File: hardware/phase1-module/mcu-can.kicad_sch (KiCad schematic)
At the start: 0 parts

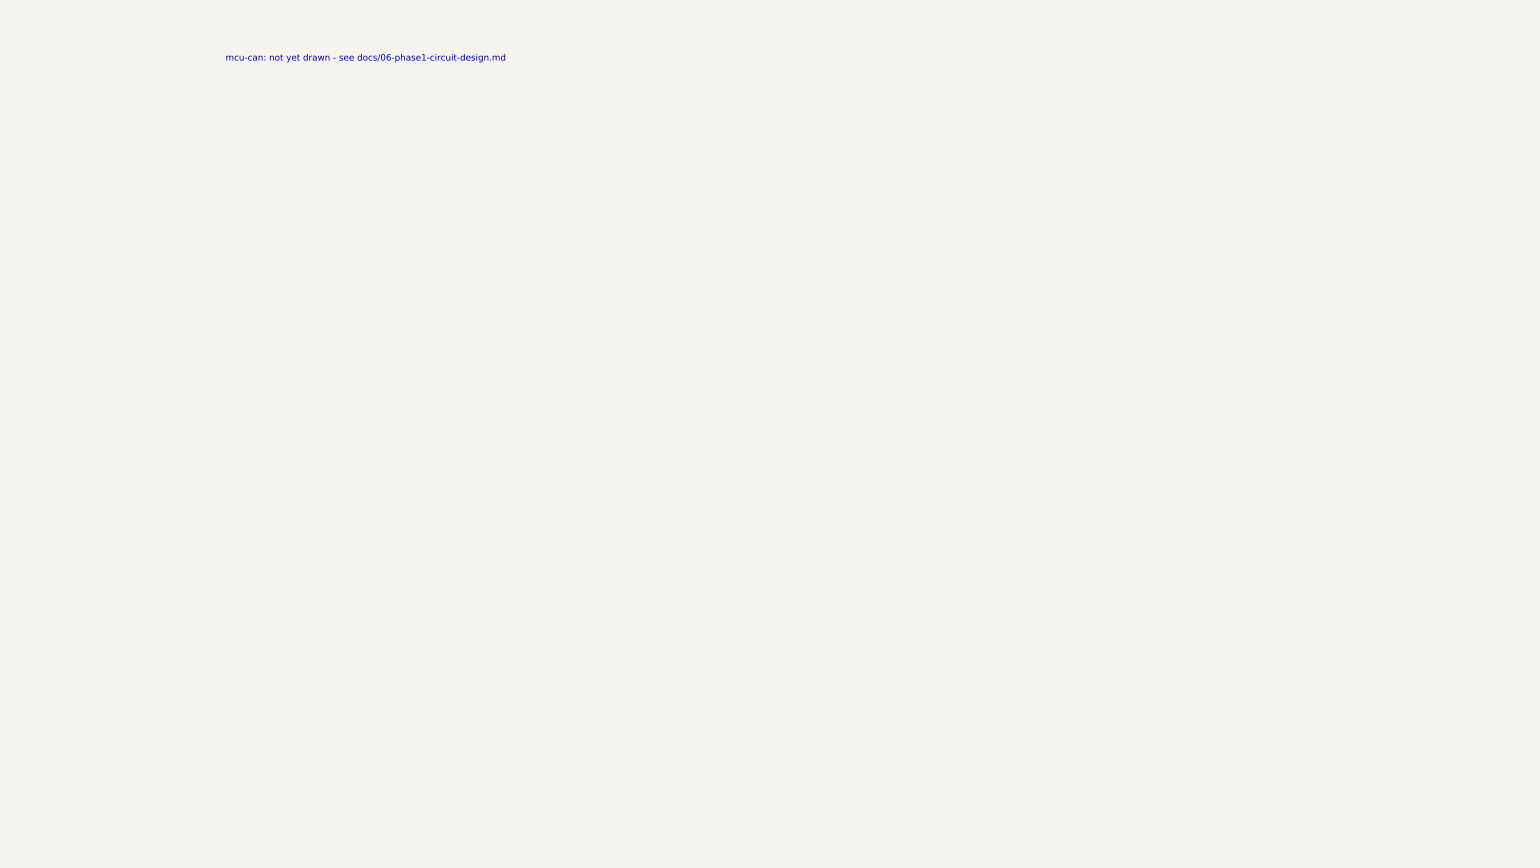
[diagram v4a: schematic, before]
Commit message: Complete Phase-1 schematic: all six remaining sheets, netlist-verified
- power-stage: LM5145 @350kHz (RT 28.7K per ds eq.3), RDS(on) valley
  ILIM 365R->SW, UVLO divider, EN kill chain (NOT(HW_EN) OR PS_OFF via
  Q5/Q6 + diode-OR), Type-III comp starting values, SYNCIN as DEM/FPWM
- sensing: 2m shunt, INA240A3 -> CC loop, INA228 telemetry, /8 divider,
  NT1 single AGND-PGND tie
- disconnect: back-to-back FETs + LTC7004, INP = OUT_REQ AND NOT(kill)
  AND NOT(OVP); TLV7011 + Q9 trips at 22.25V
- aux-rails: LMR36015 (5.016V) -> NCP1117 3V3
- mcu-can: STM32G431CBT6 fully pinned; I2C moved to I2C2/PA8-PA9 (PB8
  is the BOOT0 strap - pullup there would boot the ROM loader), BOOT0
  strapped low, OUT_REQ on PB14 (PB4 NJTRST reset pull-up), 8MHz
  crystal for CAN, TCAN1042 (VCC 5V, VIO 3V3)
- io: fused input + SMBJ33A TVS, output, backplane header, fan switch
  (1N4148W flyback orientation corrected: pin 1 = cathode)
- checker: duplicate-ref detection + global/local split-net detection;
  caught duplicate C62 and the LMR36015 FB-pin placement collision

Co-Authored-By: Claude Fable 5 <noreply@anthropic.com>
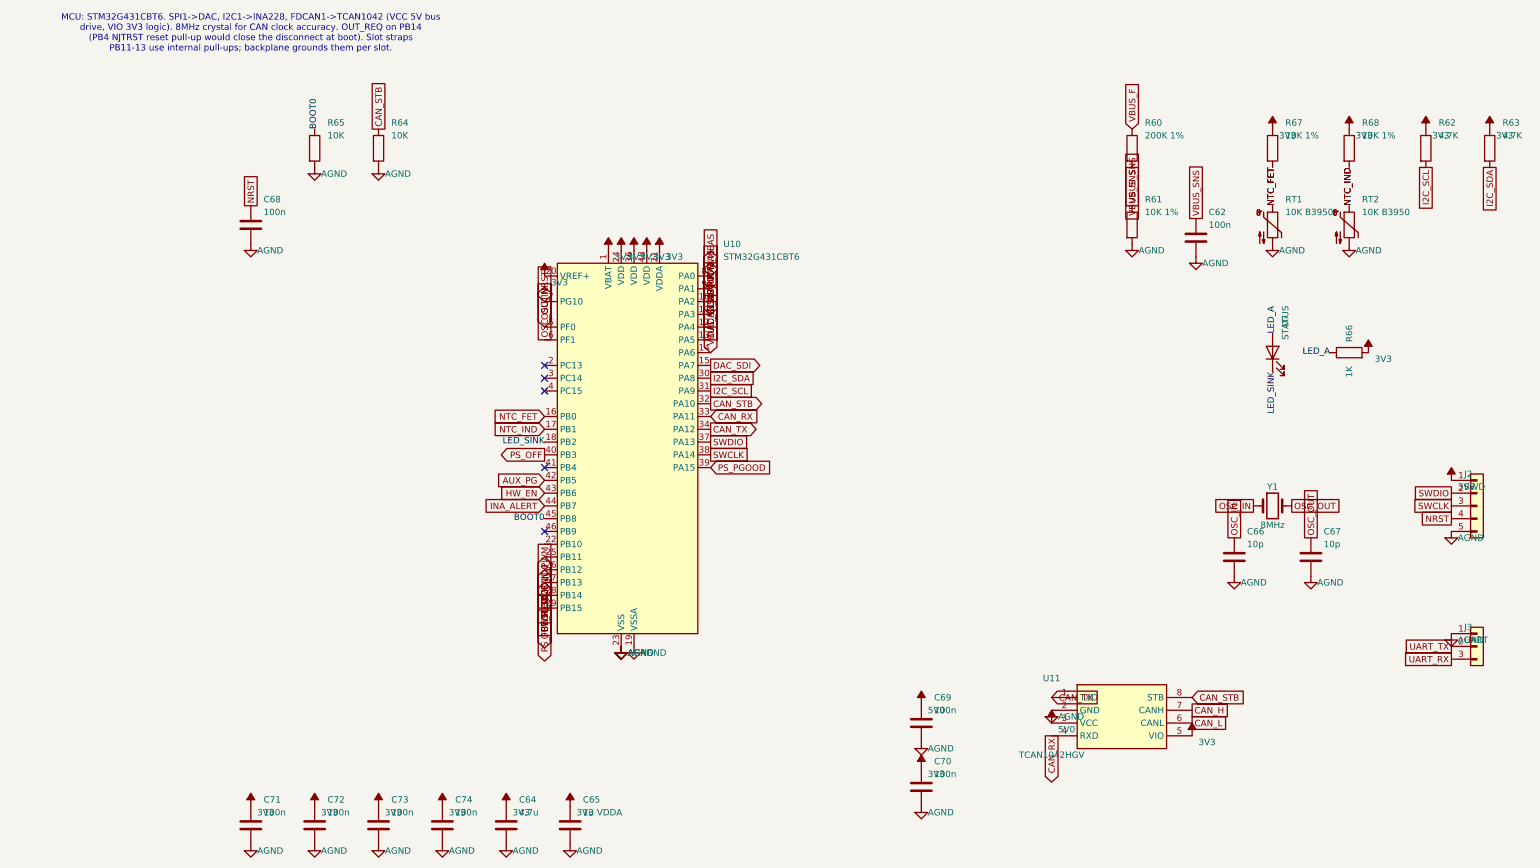
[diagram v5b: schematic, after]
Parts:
- added C62, C68, C69, C70, C71, C72, C73, C74: 100n, Capacitor_SMD:C_0402_1005Metric, symbol Device:C
- added C64: 4.7u, Capacitor_SMD:C_0402_1005Metric, symbol Device:C
- added C65: 1u VDDA, Capacitor_SMD:C_0402_1005Metric, symbol Device:C
- added C66, C67: 10p, Capacitor_SMD:C_0402_1005Metric, symbol Device:C
- added D7: STATUS, LED_SMD:LED_0603_1608Metric, symbol Device:LED
- added J2: SWD, Connector_PinHeader_2.54mm:PinHeader_1x05_P2.54mm_Vertical, symbol Connector_Generic:Conn_01x05
- added J3: UART, Connector_PinHeader_2.54mm:PinHeader_1x03_P2.54mm_Vertical, symbol Connector_Generic:Conn_01x03
- added R60: 200K 1%, Resistor_SMD:R_0402_1005Metric, symbol Device:R
- added R61, R67, R68: 10K 1%, Resistor_SMD:R_0402_1005Metric, symbol Device:R
- added R62, R63: 4.7K, Resistor_SMD:R_0402_1005Metric, symbol Device:R
- added R64, R65: 10K, Resistor_SMD:R_0402_1005Metric, symbol Device:R
- added R66: 1K, Resistor_SMD:R_0402_1005Metric, symbol Device:R
- added RT1, RT2: 10K B3950, Resistor_SMD:R_0603_1608Metric, symbol Device:Thermistor_NTC
- added U10: STM32G431CBT6, Package_QFP:LQFP-48_7x7mm_P0.5mm, symbol MCU_ST_STM32G4:STM32G431CBTx
- added U11: TCAN1042HGV, Package_SO:SOIC-8_3.9x4.9mm_P1.27mm, symbol labbench:TCAN1042HGVDR
- added Y1: 8MHz, Crystal:Crystal_SMD_3225-4Pin_3.2x2.5mm, symbol Device:Crystal
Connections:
- new net 3V3: C64.1, C65.1, C70.1, C71.1, C72.1, C73.1, C74.1, J2.1 (Pin_1), R62.1, R63.1, R66.2, R67.1, R68.1, U10.1 (VBAT), U10.20 (VREF+), U10.21 (VDDA), U10.24 (VDD), U10.36 (VDD), U10.48 (VDD), U11.5 (VIO)
- new net 5V0: C69.1, U11.3 (VCC)
- new net AGND: C62.2, C64.2, C65.2, C66.2, C67.2, C68.2, C69.2, C70.2, C71.2, C72.2, C73.2, C74.2, J2.5 (Pin_5), J3.1 (Pin_1), R61.2, R64.2, R65.2, RT1.2, RT2.2, U10.19 (VSSA), U10.23 (VSS), U10.35 (VSS), U10.47 (VSS), U11.2 (GND)
- new net AUX_PG: U10.42 (PB5)
- new net BOOT0: R65.1, U10.45 (PB8)
- new net CAN_H: U11.7 (CANH)
- new net CAN_L: U11.6 (CANL)
- new net CAN_RX: U10.33 (PA11), U11.4 (RXD)
- new net CAN_STB: R64.1, U10.32 (PA10), U11.8 (STB)
- new net CAN_TX: U10.34 (PA12), U11.1 (TXD)
- new net DAC_NSYNC: U10.12 (PA4)
- new net DAC_SCLK: U10.13 (PA5)
- new net DAC_SDI: U10.15 (PA7)
- new net FAN_PWM: U10.22 (PB10)
- new net HW_EN: U10.43 (PB6)
- new net I2C_SCL: R62.2, U10.31 (PA9)
- new net I2C_SDA: R63.2, U10.30 (PA8)
- new net INA_ALERT: U10.44 (PB7)
- new net I_MEAS: U10.9 (PA1)
- new net LED_A: D7.2 (A), R66.1
- new net LED_SINK: D7.1 (K), U10.18 (PB2)
- new net NRST: C68.1, J2.4 (Pin_4), U10.7 (PG10)
- new net NTC_FET: R67.2, RT1.1, U10.16 (PB0)
- new net NTC_IND: R68.2, RT2.1, U10.17 (PB1)
- new net OSC_IN: C66.1, U10.5 (PF0), Y1.1
- new net OSC_OUT: C67.1, U10.6 (PF1), Y1.2
- new net OUT_REQ: U10.28 (PB14)
- new net PS_FPWM: U10.29 (PB15)
- new net PS_OFF: U10.40 (PB3)
- new net PS_PGOOD: U10.39 (PA15)
- new net SLOT_ID0: U10.25 (PB11)
- new net SLOT_ID1: U10.26 (PB12)
- new net SLOT_ID2: U10.27 (PB13)
- new net SWCLK: J2.3 (Pin_3), U10.38 (PA14)
- new net SWDIO: J2.2 (Pin_2), U10.37 (PA13)
- new net UART_RX: J3.3 (Pin_3), U10.11 (PA3)
- new net UART_TX: J3.2 (Pin_2), U10.10 (PA2)
- new net VBUS_F: R60.1
- new net VBUS_SNS: C62.1, R60.2, R61.1, U10.14 (PA6)
- new net V_MEAS: U10.8 (PA0)
- no-connect marks 0 -> 5
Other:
- note added: "MCU: STM32G431CBT6. SPI1->DAC, I2C1->INA228, FDCAN1->TCAN1042 (VCC 5V bus drive, VIO 3V3 logic). 8MHz crystal for CAN clock accuracy. OUT_REQ on PB14 (PB4 NJTRST reset pull-up would close the disconnect at boot). Slot straps PB11-13 use internal pull-ups; backplane grounds them per slot."
- note removed: "mcu-can: not yet drawn - see docs/06-phase1-circuit-design.md"

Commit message: Footprint pass: labbench.pretty library, all 137 components verified
- build_fplib.py: merges vetted vendor footprints (LM5145 RGY0020B,
  LMR36015 RNX, DAC80502 WSON-10 no-EP) and generates PowerFET_SON5x6_GDS
  from the TI Q5A land pattern (CSD18563Q5A SLPS444C) with pads renumbered
  1=G/2=D/3=S to match the generic NMOS symbol; writes fp-lib-table.
- check_footprints.py: every component must have a resolvable footprint and
  every netted pin a matching pad (caught a wrong official VSSOP-8 name).
- gen_phase1.py: passives 0402->0603 (hand assembly); DAC80502 vendor fp
  (DRX has no exposed pad); L1 = Coilcraft XAL1350-103ME on official fp;
  net-tie fp; crystal -> Crystal_GND24 with grounded shield pads; bulk cap
  banks expanded to one component per physical cap (C75-C81); R27 preload
  1W -> 2512.
- PARTS-TO-DOWNLOAD.md section D: new orderables for the footprint pass.

check_netlist + check_footprints: all OK (137 components).

Co-Authored-By: Claude Fable 5 <noreply@anthropic.com>
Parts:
- removed Y1: 8MHz, Crystal:Crystal_SMD_3225-4Pin_3.2x2.5mm, symbol Device:Crystal
- added Y1: 8MHz, Crystal:Crystal_SMD_3225-4Pin_3.2x2.5mm, symbol Device:Crystal_GND24
- C62, C64, C65, C66, C67, C68, C69, C70, C71, C72, C73, C74: footprint Capacitor_SMD:C_0402_1005Metric -> Capacitor_SMD:C_0603_1608Metric
- R60, R61, R62, R63, R64, R65, R66, R67, R68: footprint Resistor_SMD:R_0402_1005Metric -> Resistor_SMD:R_0603_1608Metric
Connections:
- net AGND: now also Y1.2, Y1.4
- net OSC_IN: now also Y1.1
- net OSC_OUT: now also Y1.3
